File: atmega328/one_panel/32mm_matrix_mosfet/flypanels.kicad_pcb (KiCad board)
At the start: 2 copper layers, 32 x 32 mm, 16 parts, among them IC1 ATMEGA328-A, P1 CONN_8, P2 CONN_8, X1 CER_RESO

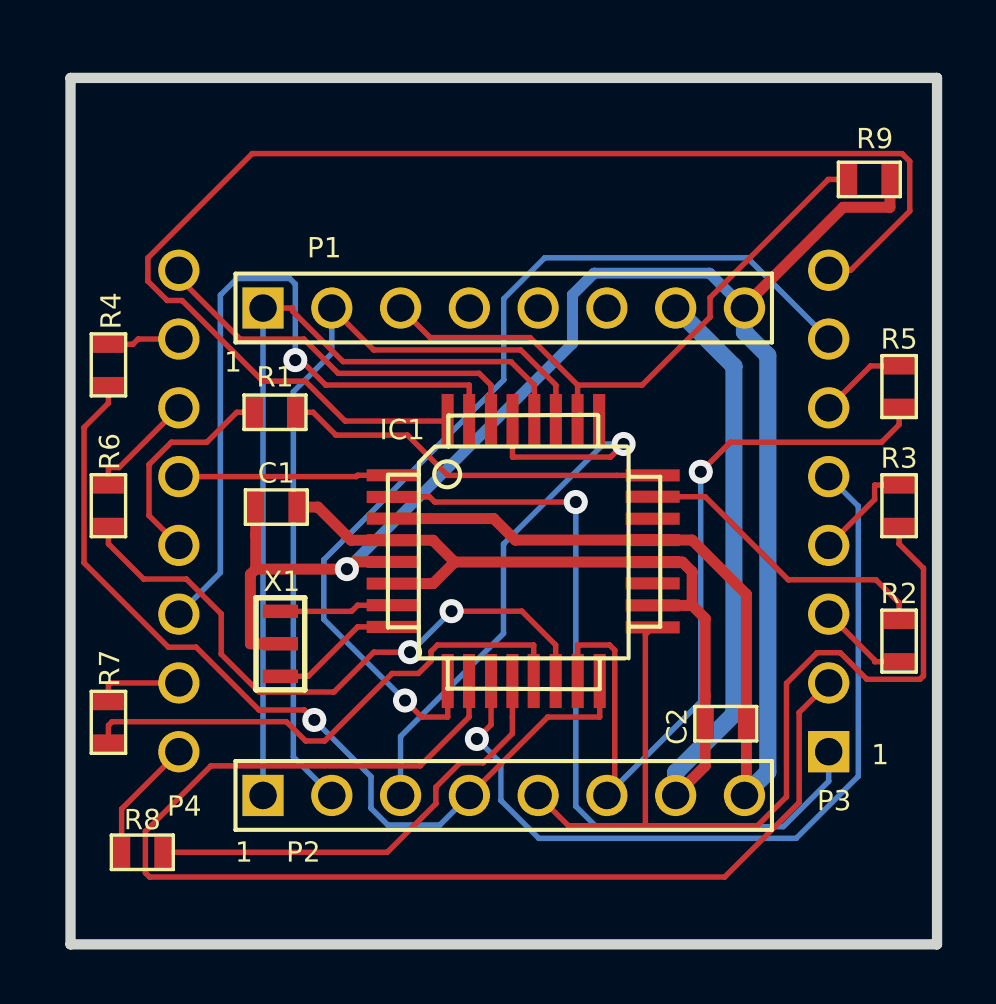
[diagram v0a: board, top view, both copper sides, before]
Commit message: Added version of single matrix atmega328 design with mosfets.
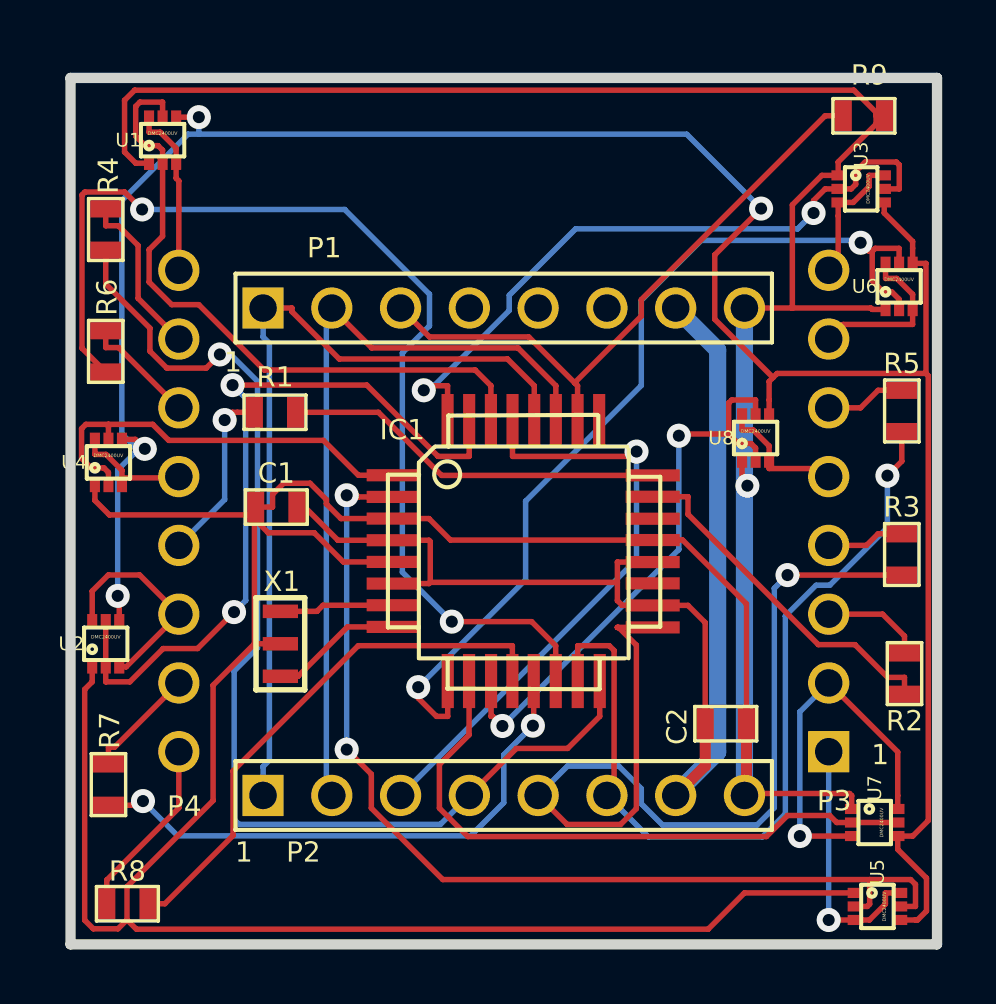
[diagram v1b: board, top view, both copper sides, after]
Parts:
- added U1: DMC2400UV, DMC2400UV, F.Cu at (103.4, 70.3)
- added U2: DMC2400UV, DMC2400UV, F.Cu at (101.3, 88.9)
- added U3: DMC2400UV, DMC2400UV, F.Cu at (129.2, 72.1)
- added U4: DMC2400UV, DMC2400UV, F.Cu at (101.4, 82.2)
- added U5: DMC2400UV, DMC2400UV, F.Cu at (129.8, 98.6)
- added U6: DMC2400UV, DMC2400UV, F.Cu at (130.6, 75.7)
- added U7: DMC2400UV, DMC2400UV, F.Cu at (129.7, 95.5)
- added U8: DMC2400UV, DMC2400UV, F.Cu at (125.3, 81.3)
- moved R6 5.70 mm to (101.3, 78.1)
- moved R4 5.00 mm to (101.3, 73.6)
- moved R9 2.36 mm to (129.3, 69.4)
- moved R7 2.30 mm to (101.4, 94.1)
- moved R8 1.98 mm to (102.1, 98.5)
- moved R3 1.80 mm to (130.7, 85.6)
- moved R2 1.22 mm to (130.8, 90.0), turned to 270 degrees
- moved R5 0.91 mm to (130.7, 80.3)
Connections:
- IC1 pad 1: N-0000030 (its old number) -> /D3
- IC1 pad 10: N-0000021 (its old number) -> /D6
- IC1 pad 11: N-000003 -> /D7
- IC1 pad 19: N-0000027 (its old number) -> (no net)
- IC1 pad 2: N-0000020 (its old number) -> /D4
- IC1 pad 22: N-0000026 (its old number) -> (no net)
- IC1 pad 25: N-0000012 -> (no net)
- IC1 pad 30: N-0000013 -> /D0
- IC1 pad 31: N-000002 -> /D1
- IC1 pad 32: N-0000019 (its old number) -> /D2
- IC1 pad 9: N-0000025 (its old number) -> /D5
- MATRIX1 pad 1: N-0000020 (its old number) -> /CAT4
- MATRIX1 pad 12: N-0000030 (its old number) -> /CAT5
- MATRIX1 pad 14: N-000002 -> /CAT7
- MATRIX1 pad 2: N-0000021 (its old number) -> /CAT2
- MATRIX1 pad 5: N-000003 -> /CAT1
- MATRIX1 pad 7: N-0000025 (its old number) -> /CAT3
- MATRIX1 pad 8: N-0000019 (its old number) -> /CAT6
- MATRIX1 pad 9: N-0000013 -> /CAT8
- P1 pad 4: N-0000033 (its old number) -> (no net)
- P1 pad 5: N-0000032 (its old number) -> (no net)
- P1 pad 6: N-0000031 (its old number) -> (no net)
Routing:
- net +5V: track 0.00 -> 89.0 mm, vias 0 -> 4
- net GND: track 80.6 -> 168.5 mm
- net N-0000019 (its old number): track 49.7 -> 0.00 mm
- net N-0000021 (its old number): track 46.8 -> 0.00 mm
- net /D4: track 0.00 -> 37.8 mm, vias 0 -> 2
- net N-0000025 (its old number): track 35.9 -> 0.00 mm, vias 1 -> 0
- net /D5: track 0.00 -> 34.7 mm, vias 0 -> 2
- net N-000003: track 31.2 -> 0.00 mm, vias 1 -> 0
- net N-0000020 (its old number): track 29.5 -> 0.00 mm, vias 1 -> 0
- net /D1: track 0.00 -> 28.0 mm, vias 0 -> 2
- net N-000002: track 26.5 -> 0.00 mm, vias 1 -> 0
- net /D2: track 0.00 -> 25.7 mm, vias 0 -> 2
- net /D0: track 0.00 -> 24.5 mm
- net /D6: track 0.00 -> 22.9 mm
- net /D7: track 0.00 -> 21.6 mm, vias 0 -> 2
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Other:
- net class Default: clearance 0.2286 -> 0.2032
- net class VCC: clearance 0.254 -> 0.2032; trace_width 0.4064 -> 0.2032
- rule trace_clearance: 0.2286 -> 0.2032

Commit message: Added gerber files file flypanels 32mm matrix atmega328 w/ MOSFET.
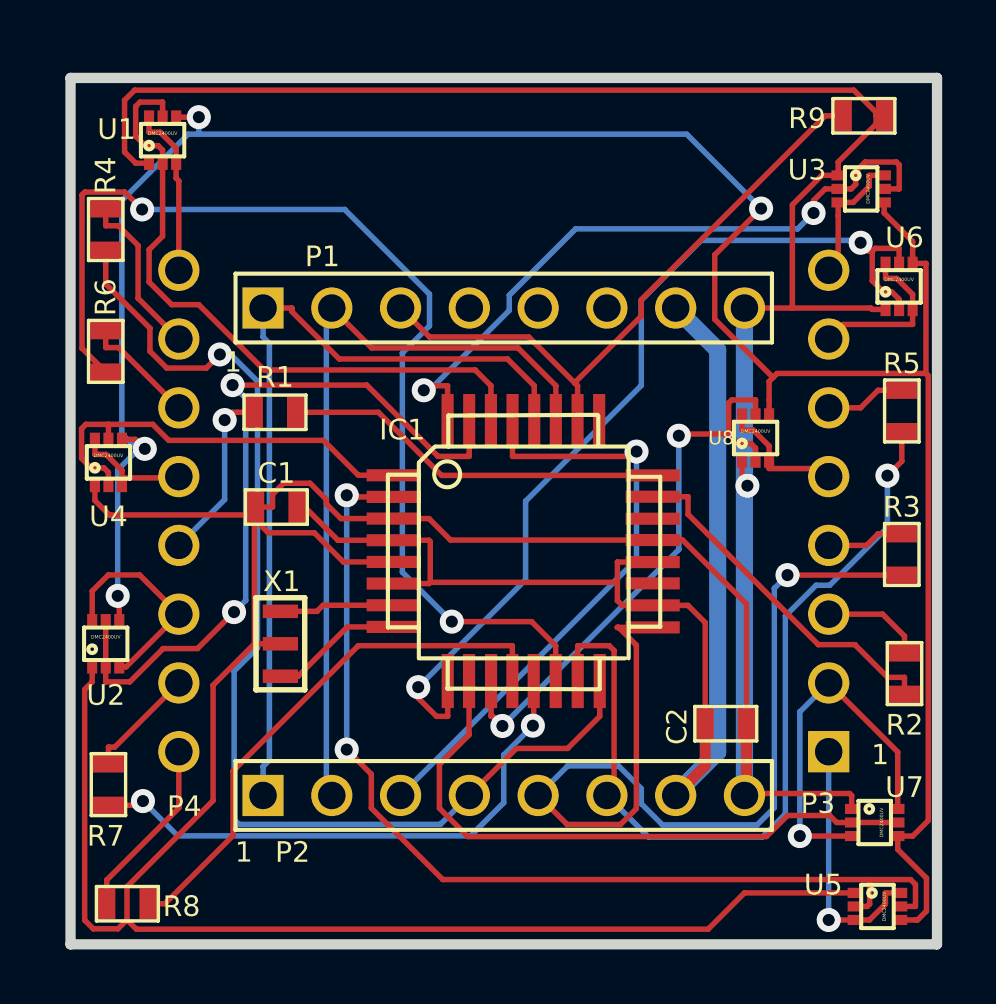
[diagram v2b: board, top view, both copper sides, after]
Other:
- board text added: "BOT"
- board text added: "Flypanel v3.0 R1 www.iorodeo.com"
- board text removed: "Flypanel v2.0 www.iorodeo.com"
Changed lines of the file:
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@@
     (links 90)
     (no_connects 0)
-    (area 99.211556 67.24608 132.354061 100.352861)
+    (area 99.643939 67.642739 132.354061 100.352861)
     (thickness 1.6002)
-    (drawings 11)
+    (drawings 12)
     (tracks 503)
     (zones 0)
@@
     (pcb_text_size 1.524 2.032)
     (mod_edge_width 0.2032)
-    (mod_text_size 1.524 1.524)
+    (mod_text_size 0.762 0.762)
     (mod_text_width 0.1524)
     (pad_size 0.375 0.5)
@@
       (drillshape 0)
       (scaleselection 1)
-      (outputdirectory gerber_v2p0_oshpark/))
+      (outputdirectory gerber_v3.0r1/))
   )
   (net 0 "")
@@
     (at 129.3 69.4)
     (attr smd)
-    (fp_text reference R9 (at 0.20066 -1.50114) (layer F.SilkS)
-      (effects (font (size 0.7493 0.7493) (thickness 0.14986)))
+    (fp_text reference R9 (at -2.1 0.1) (layer F.SilkS)
+      (effects (font (size 0.762 0.762) (thickness 0.1524)))
     )
     (fp_text value 10K (at 0 0) (layer F.SilkS) hide
@@
     (at 102.1 98.5)
     (attr smd)
-    (fp_text reference R8 (at 0 -1.2) (layer F.SilkS)
-      (effects (font (size 0.7493 0.7493) (thickness 0.14986)))
+    (fp_text reference R8 (at 2 0.1) (layer F.SilkS)
+      (effects (font (size 0.762 0.762) (thickness 0.1524)))
     )
     (fp_text value 150 (at 0 0) (layer F.SilkS) hide
@@
     (at 101.4 94.1 270)
     (attr smd)
-    (fp_text reference R7 (at -2 -0.05 270) (layer F.SilkS)
-      (effects (font (size 0.7493 0.7493) (thickness 0.14986)))
+    (fp_text reference R7 (at 1.9 0.1 360) (layer F.SilkS)
+      (effects (font (size 0.762 0.762) (thickness 0.1524)))
     )
     (fp_text value 150 (at 0 0 270) (layer F.SilkS) hide
@@
     (at 101.3 78.1 270)
     (attr smd)
-    (fp_text reference R6 (at -2 -0.05 270) (layer F.SilkS)
-      (effects (font (size 0.7493 0.7493) (thickness 0.14986)))
+    (fp_text reference R6 (at -2 0 270) (layer F.SilkS)
+      (effects (font (size 0.762 0.762) (thickness 0.1524)))
     )
     (fp_text value 150 (at 0 0 270) (layer F.SilkS) hide
@@
     (attr smd)
     (fp_text reference R5 (at -1.75 0 360) (layer F.SilkS)
-      (effects (font (size 0.7493 0.7493) (thickness 0.14986)))
+      (effects (font (size 0.762 0.762) (thickness 0.1524)))
     )
     (fp_text value 150 (at 0 0 270) (layer F.SilkS) hide
@@
     (at 101.3 73.6 270)
     (attr smd)
-    (fp_text reference R4 (at -2 -0.1 270) (layer F.SilkS)
-      (effects (font (size 0.7493 0.7493) (thickness 0.14986)))
+    (fp_text reference R4 (at -2 0 270) (layer F.SilkS)
+      (effects (font (size 0.762 0.762) (thickness 0.1524)))
     )
     (fp_text value 150 (at 0 0 270) (layer F.SilkS) hide
@@
     (attr smd)
     (fp_text reference R3 (at -1.75 0 360) (layer F.SilkS)
-      (effects (font (size 0.7493 0.7493) (thickness 0.14986)))
+      (effects (font (size 0.762 0.762) (thickness 0.1524)))
     )
     (fp_text value 150 (at 0 0 270) (layer F.SilkS) hide
@@
     (at 130.8 90 270)
     (attr smd)
-    (fp_text reference R2 (at 1.75 0 360) (layer F.SilkS)
-      (effects (font (size 0.7493 0.7493) (thickness 0.14986)))
+    (fp_text reference R2 (at 1.9 0 360) (layer F.SilkS)
+      (effects (font (size 0.762 0.762) (thickness 0.1524)))
     )
     (fp_text value 150 (at 0 0 270) (layer F.SilkS) hide
@@
     (attr smd)
     (fp_text reference R1 (at 0 -1.3) (layer F.SilkS)
-      (effects (font (size 0.7493 0.7493) (thickness 0.14986)))
+      (effects (font (size 0.762 0.762) (thickness 0.1524)))
     )
     (fp_text value 150 (at 0 0) (layer F.SilkS) hide
@@
     (at 116.75 85.5)
     (fp_text reference IC1 (at -4.50088 -4.50088) (layer F.SilkS)
-      (effects (font (size 0.7493 0.7493) (thickness 0.14986)))
+      (effects (font (size 0.762 0.762) (thickness 0.1524)))
     )
     (fp_text value ATMEGA328-A (at -0.39878 7.0993) (layer F.SilkS) hide
@@
     (attr smd)
     (fp_text reference C1 (at 0 1.25 180) (layer F.SilkS)
-      (effects (font (size 0.7493 0.7493) (thickness 0.14986)))
+      (effects (font (size 0.762 0.762) (thickness 0.1524)))
     )
     (fp_text value 0.1uF (at 0 0 180) (layer F.SilkS) hide
@@
     (descr "Pin connector 8x1")
     (tags CONN)
-    (fp_text reference P1 (at -6.6294 -2.21996) (layer F.SilkS)
-      (effects (font (size 0.7493 0.7493) (thickness 0.14986)))
+    (fp_text reference P1 (at -6.699 -1.8997) (layer F.SilkS)
+      (effects (font (size 0.762 0.762) (thickness 0.1524)))
     )
     (fp_text value CONN_8 (at 0 3.302) (layer F.SilkS) hide
@@
     (descr "Pin connector 8x1")
     (tags CONN)
-    (fp_text reference P2 (at -7.39902 2.09804) (layer F.SilkS)
-      (effects (font (size 0.7493 0.7493) (thickness 0.14986)))
+    (fp_text reference P2 (at -7.799 2.0993) (layer F.SilkS)
+      (effects (font (size 0.762 0.762) (thickness 0.1524)))
     )
     (fp_text value CONN_8 (at 0 3.302) (layer F.SilkS) hide
@@
     (tags "Resonator, Ceramic")
     (fp_text reference X1 (at -2.3 -0.05 360) (layer F.SilkS)
-      (effects (font (size 0.7493 0.7493) (thickness 0.14986)))
+      (effects (font (size 0.762 0.762) (thickness 0.1524)))
     )
     (fp_text value CER_RESO (at 0.8001 2.4003 270) (layer F.SilkS) hide
@@
   (module DMC2400UV (layer Front)
     (at 103.4 70.3)
-    (fp_text reference U1 (at -1.27 0) (layer F.SilkS)
-      (effects (font (size 0.508 0.508) (thickness 0.1016)))
+    (fp_text reference U1 (at -1.7 -0.4) (layer F.SilkS)
+      (effects (font (size 0.762 0.762) (thickness 0.1524)))
     )
     (fp_text value DMC2400UV (at 0 -0.254) (layer F.SilkS)
@@
   (module DMC2400UV (layer Front)
     (at 101.3 88.9)
-    (fp_text reference U2 (at -1.27 0) (layer F.SilkS)
-      (effects (font (size 0.508 0.508) (thickness 0.1016)))
+    (fp_text reference U2 (at 0 1.9) (layer F.SilkS)
+      (effects (font (size 0.762 0.762) (thickness 0.1524)))
     )
     (fp_text value DMC2400UV (at 0 -0.254) (layer F.SilkS)
@@
   (module DMC2400UV (layer Front)
     (at 129.2 72.1 270)
-    (fp_text reference U3 (at -1.27 0 270) (layer F.SilkS)
-      (effects (font (size 0.508 0.508) (thickness 0.1016)))
+    (fp_text reference U3 (at -0.7 2 360) (layer F.SilkS)
+      (effects (font (size 0.762 0.762) (thickness 0.1524)))
     )
     (fp_text value DMC2400UV (at 0 -0.254 270) (layer F.SilkS)
@@
   (module DMC2400UV (layer Front)
     (at 101.4 82.2)
-    (fp_text reference U4 (at -1.27 0) (layer F.SilkS)
-      (effects (font (size 0.508 0.508) (thickness 0.1016)))
+    (fp_text reference U4 (at 0 2) (layer F.SilkS)
+      (effects (font (size 0.762 0.762) (thickness 0.1524)))
     )
     (fp_text value DMC2400UV (at 0 -0.254) (layer F.SilkS)
@@
   (module DMC2400UV (layer Front)
     (at 129.8 98.6 270)
-    (fp_text reference U5 (at -1.27 0 270) (layer F.SilkS)
-      (effects (font (size 0.508 0.508) (thickness 0.1016)))
+    (fp_text reference U5 (at -0.8 2 360) (layer F.SilkS)
+      (effects (font (size 0.762 0.762) (thickness 0.1524)))
     )
     (fp_text value DMC2400UV (at 0 -0.254 270) (layer F.SilkS)
@@
   (module DMC2400UV (layer Front)
     (at 130.6 75.7)
-    (fp_text reference U6 (at -1.27 0) (layer F.SilkS)
-      (effects (font (size 0.508 0.508) (thickness 0.1016)))
+    (fp_text reference U6 (at 0.2 -1.8) (layer F.SilkS)
+      (effects (font (size 0.762 0.762) (thickness 0.1524)))
     )
     (fp_text value DMC2400UV (at 0 -0.254) (layer F.SilkS)
@@
   (module DMC2400UV (layer Front)
     (at 129.7 95.5 270)
-    (fp_text reference U7 (at -1.27 0 270) (layer F.SilkS)
-      (effects (font (size 0.508 0.508) (thickness 0.1016)))
+    (fp_text reference U7 (at -1.3 -1.1 360) (layer F.SilkS)
+      (effects (font (size 0.762 0.762) (thickness 0.1524)))
     )
     (fp_text value DMC2400UV (at 0 -0.254 270) (layer F.SilkS)
@@
     )
   )
-  (gr_text P3 (at 128.20142 94.70136) (layer F.SilkS)
+  (gr_text BOT (at 129.8 99.1) (layer B.SilkS)
+    (effects (font (size 1.016 1.016) (thickness 0.2032)) (justify mirror))
+  )
+  (gr_text P3 (at 127.6 94.8) (layer F.SilkS)
     (effects (font (size 0.7493 0.7493) (thickness 0.14986)))
   )
@@
   (gr_line (start 99.9998 68.00088) (end 132.00126 68.00088) (angle 90) (layer Edge.Cuts) (width 0.381))
   (gr_line (start 99.9998 99.9998) (end 99.9998 68.00088) (angle 90) (layer Edge.Cuts) (width 0.381))
-  (gr_text "Flypanel v2.0\nwww.iorodeo.com" (at 116.8 69.8) (layer B.SilkS)
+  (gr_text "Flypanel v3.0 R1\nwww.iorodeo.com" (at 116.8 69.8) (layer B.SilkS)
     (effects (font (size 1.00076 1.00076) (thickness 0.20066)) (justify mirror))
   )

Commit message: Added gerber files for 2nd revision of one matrix atmeg328.
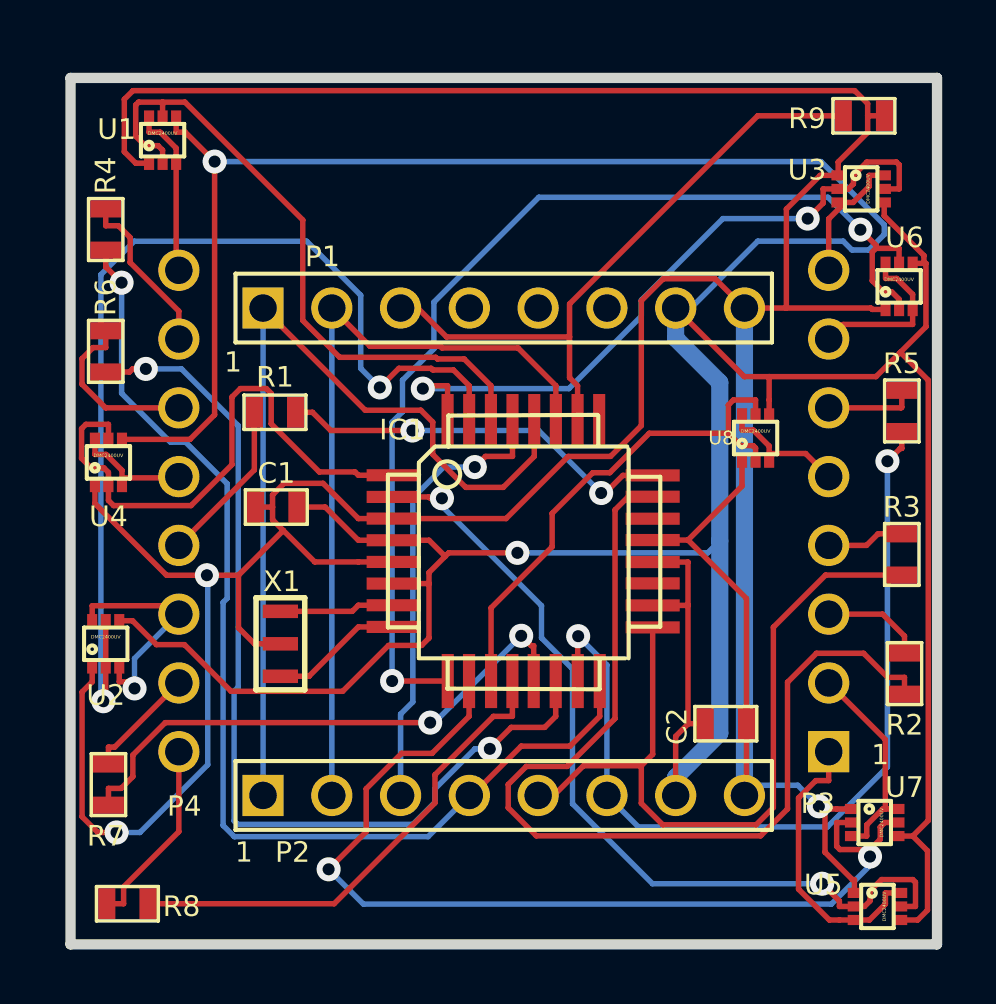
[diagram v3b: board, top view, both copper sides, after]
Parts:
- R1, R2, R3, R4, R5, R6, R7, R8: value 150 -> 160
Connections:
- C1 pad 1: VCC -> +5V
- C2 pad 1: VCC -> +5V
- IC1 pad 18: VCC -> +5V
- IC1 pad 20: VCC -> +5V
- IC1 pad 4: VCC -> +5V
- IC1 pad 6: VCC -> +5V
- P1 pad 7: VCC -> +5V
- P2 pad 7: VCC -> +5V
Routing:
- net +5V: track 89.0 -> 158.2 mm, vias 4 -> 2
- net VCC: track 47.7 -> 0.00 mm
- net N-0000031: track 13.1 -> 36.7 mm
- net GND: track 168.5 -> 150.6 mm, vias 1 -> 3
- net /D6: track 22.9 -> 35.9 mm, vias 0 -> 2
- net /D1: track 28.0 -> 38.6 mm
- net N-0000019: track 36.3 -> 28.6 mm, vias 1 -> 0
- net /D4: track 37.8 -> 31.6 mm
- net /CAT2: track 13.7 -> 7.88 mm, vias 1 -> 0
- net N-0000024: track 22.3 -> 16.8 mm
- net /D3: track 15.7 -> 20.8 mm
- net /D5: track 34.7 -> 39.8 mm
- net N-0000030: track 40.1 -> 35.6 mm
- net N-0000025: track 30.8 -> 33.2 mm
- net /D7: track 21.6 -> 19.3 mm, vias 2 -> 0
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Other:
- board text added: "Flypanel v3.0 R2 www.iorodeo.com"
- board text removed: "Flypanel v3.0 R1 www.iorodeo.com"
